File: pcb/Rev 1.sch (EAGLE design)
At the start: 256 parts, among them J1 3220-10-0100-00, J2 10118194-0001LF, J3 B2B-PH-K-S(LF)(SN), Q1 MMBT3904,215MMBT3904,215, Q10 MMBT3904,215MMBT3904,215, Q11 MMBT3904,215MMBT3904,215, Q12 MMBT3904,215MMBT3904,215, Q13 MMBT3904,215MMBT3904,215, Q14 MMBT3904,215MMBT3904,215, Q15 MMBT3904,215MMBT3904,215, Q16 TEFT4300, Q17 TEFT4300, Q18 TEFT4300, Q19 TEFT4300, Q2 MMBT3904,215MMBT3904,215, Q20 MMBT3904,215MMBT3904,215, Q21 MMBT3904,215MMBT3904,215, Q22 MMBT3904,215MMBT3904,215, Q23 MMBT3904,215MMBT3904,215, Q24 TEFT4300, Q25 TEFT4300, Q26 TEFT4300, Q27 TEFT4300, Q28 SI7157DP, Q29 SI7157DP, Q3 MMBT3904,215MMBT3904,215, Q30 MMBT3906, Q31 MMBT3906, Q32 SI7157DP, Q33 MMBT3906, Q34 MMBT3906, Q4 MMBT3904,215MMBT3904,215, Q5 MMBT3904,215MMBT3904,215, Q6 MMBT3904,215MMBT3904,215, Q7 MMBT3904,215MMBT3904,215, Q8 MMBT3904,215MMBT3904,215, Q9 MMBT3904,215MMBT3904,215, SW1 210-10MS, U1 ATSAMD21G18A-MU, U10 DRV8871, U2 AP3441, U3 TPS61089, U4 BNO055, U5 MCP73811, U7 DRV8871, U8 DRV8871, U9 DRV8871

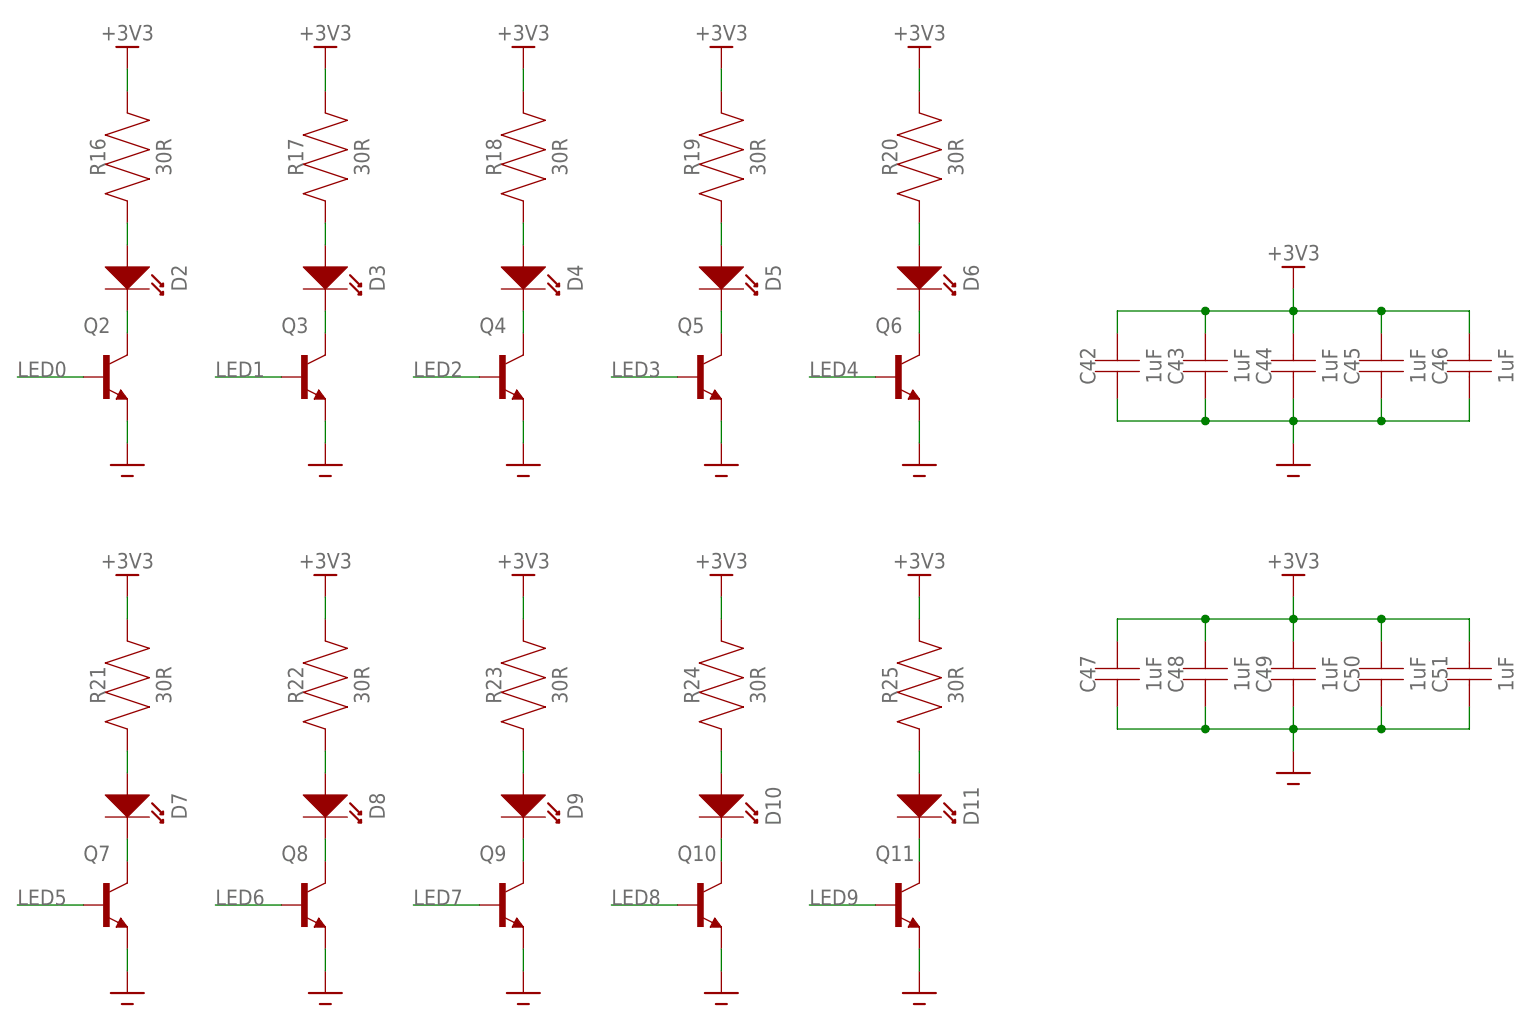
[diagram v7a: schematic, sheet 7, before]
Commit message: Placed the rest of the components
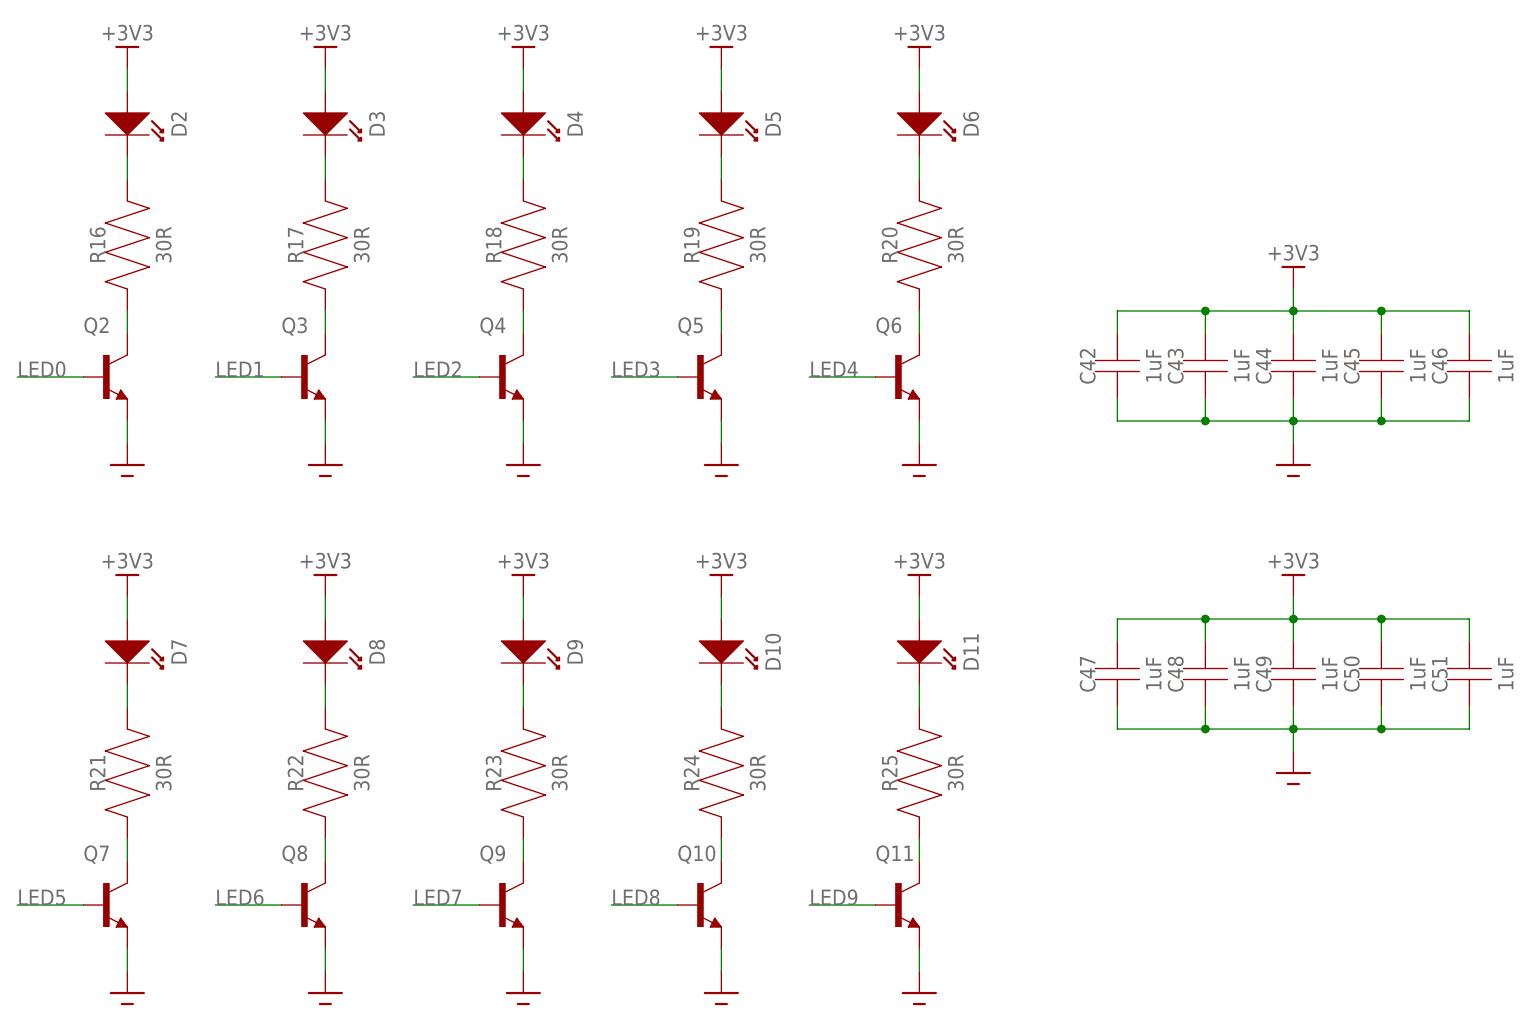
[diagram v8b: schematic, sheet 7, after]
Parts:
- removed R67, R68, R70: 10k, Micromouse 2020:RESISTOR0603
- removed R69: 10k\, Micromouse 2020:RESISTOR0603
- removed R77, R78, R79, R80: 470k, Micromouse 2020:RESISTOR0603
- C42, C43, C44, C45, C46, C47, C48, C49, C50, C51: device Micromouse 2020:CAPACITOR0805 -> Micromouse 2020:CAPACITOR0603
- R16, R17, R18, R19, R20, R21, R22, R23, R24, R25: device Micromouse 2020:RESISTOR0805 -> Micromouse 2020:RESISTOR0603
- SW1: value 210-10MS -> 210-6MS; device Micromouse 2020:210-10MS -> Micromouse 2020:210-6MS
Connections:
- removed net N$94: R67.P$2, SW1.10B
- removed net N$95: R68.P$2, SW1.9B
- removed net N$96: R69.P$2, SW1.8B
- removed net N$97: R70.P$2, SW1.7B
- removed net SW6: R80.P$1, SW1.7A
- removed net SW7: R79.P$1, SW1.8A
- removed net SW8: R78.P$1, SW1.9A
- removed net SW9: R77.P$1, SW1.10A
- net +3V3: now also D10.IN, D11.IN, D2.IN, D3.IN, D4.IN, D5.IN, D6.IN, D7.IN, D8.IN, D9.IN; no longer R16.P$2, R17.P$2, R18.P$2, R19.P$2, R20.P$2, R21.P$2, R22.P$2, R23.P$2, R24.P$2, R25.P$2, R77.P$2, R78.P$2, R79.P$2, R80.P$2
- net GND: no longer R67.P$1, R68.P$1, R69.P$1, R70.P$1
- net N$20: now also R16.P$1; no longer D2.OUT
- net N$21: now also Q3.C, R17.P$1; no longer D2.IN, R16.P$1
- net N$22: now also Q4.C, R18.P$1; no longer D3.OUT, Q3.C
- net N$23: now also Q5.C, R19.P$1; no longer D3.IN, R17.P$1
- net N$24: now also Q6.C, R20.P$1; no longer D4.OUT, Q4.C
- net N$25: now also D2.OUT, R16.P$2; no longer D4.IN, R18.P$1
- net N$26: now also D3.OUT, R17.P$2; no longer D5.OUT, Q5.C
- net N$27: now also D4.OUT, R18.P$2; no longer D5.IN, R19.P$1
- net N$28: now also D5.OUT, R19.P$2; no longer D6.OUT, Q6.C
- net N$29: now also D6.OUT, R20.P$2; no longer D6.IN, R20.P$1
- net N$30: now also R21.P$1; no longer D7.OUT
- net N$31: now also Q8.C, R22.P$1; no longer D7.IN, R21.P$1
- net N$32: now also Q9.C, R23.P$1; no longer D8.OUT, Q8.C
- net N$33: now also Q10.C, R24.P$1; no longer D8.IN, R22.P$1
- net N$34: now also Q11.C, R25.P$1; no longer D9.OUT, Q9.C
- net N$35: now also D7.OUT, R21.P$2; no longer D9.IN, R23.P$1
- net N$36: now also D8.OUT, R22.P$2; no longer D10.OUT, Q10.C
- net N$37: now also D9.OUT, R23.P$2; no longer D10.IN, R24.P$1
- net N$38: now also D10.OUT, R24.P$2; no longer D11.OUT, Q11.C
- net N$39: now also D11.OUT, R25.P$2; no longer D11.IN, R25.P$1
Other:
- moved on the sheet: D10, D11, D2, D3, D4, D5, D6, D7, D8, D9, R16, R17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
